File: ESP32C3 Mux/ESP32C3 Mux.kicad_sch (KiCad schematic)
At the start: 8 parts, among them J1 6130XX243121_613020243121, J2 Conn_01x02_Socket, U1 ESP32C3, U8 STLQ015M33R

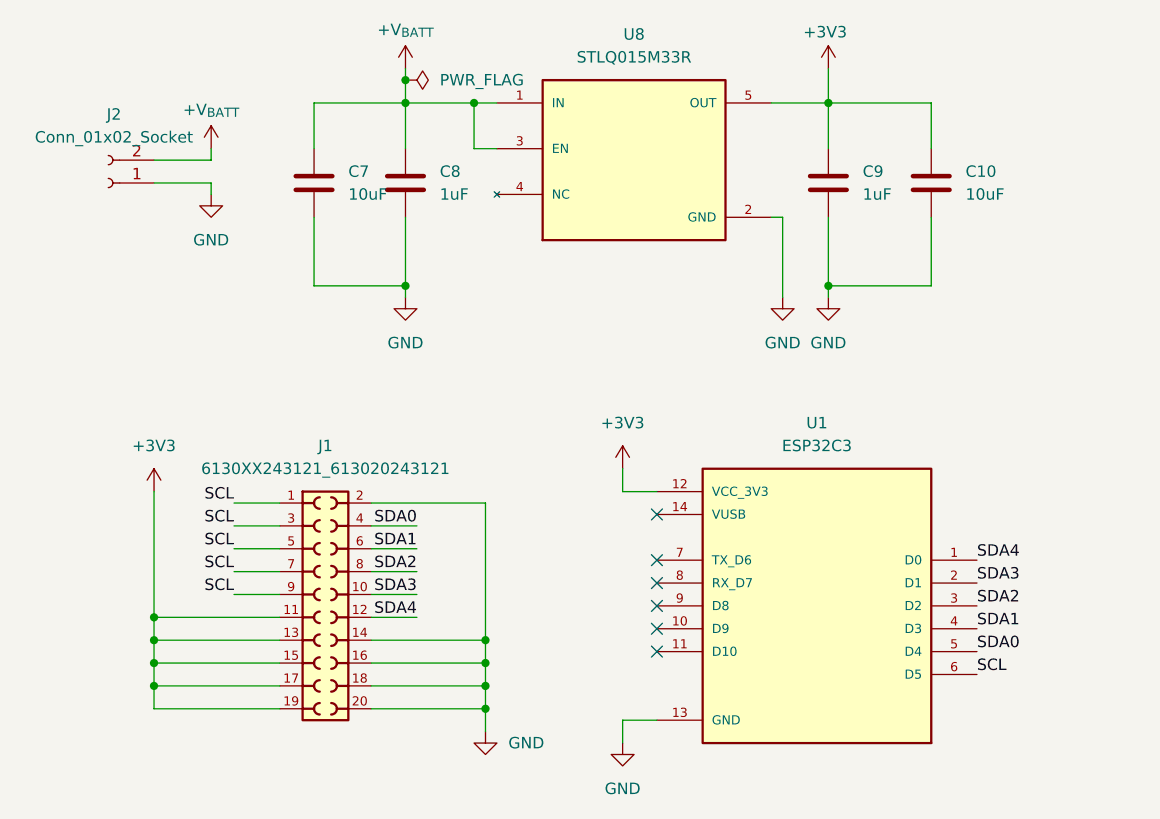
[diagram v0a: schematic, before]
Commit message: Fixed battery issues, removed LDOs
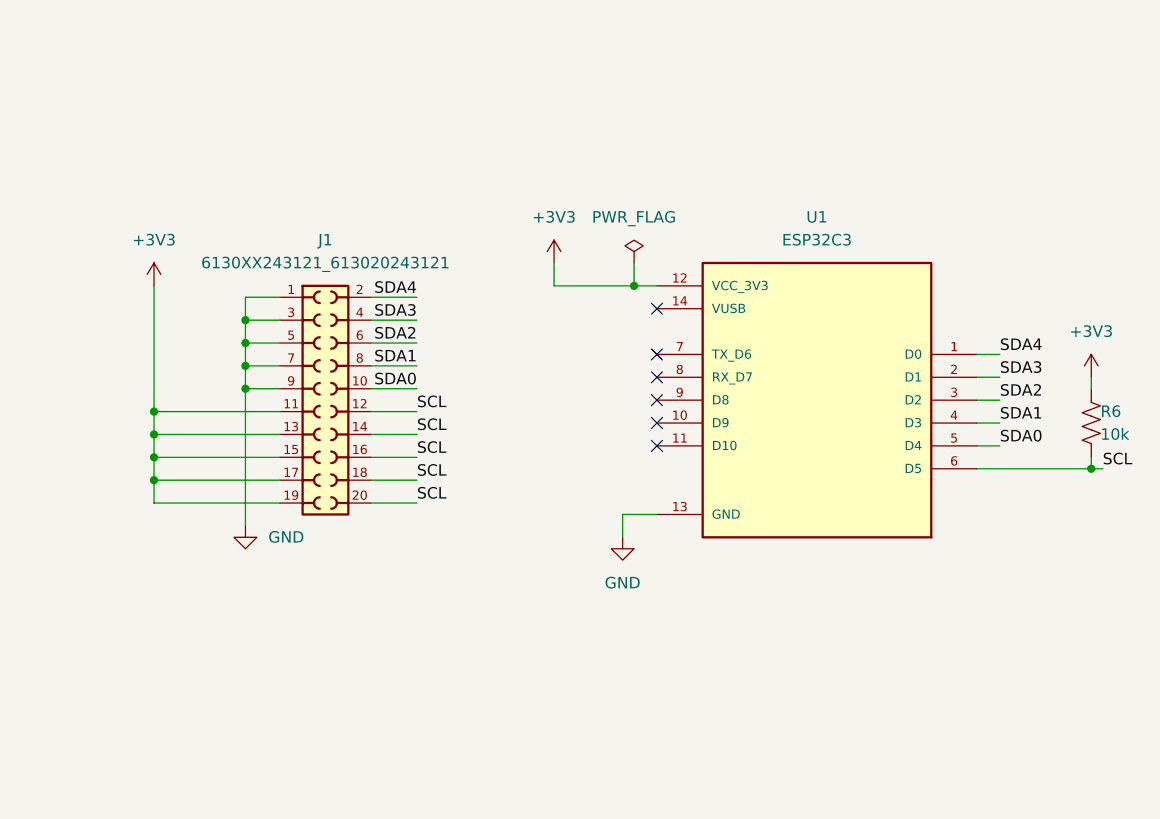
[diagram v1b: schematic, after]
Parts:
- removed C10, C7: 10uF, Capacitor_SMD:C_0805_2012Metric_Pad1.18x1.45mm_HandSolder, symbol Device:C
- removed C8, C9: 1uF, Capacitor_SMD:C_0805_2012Metric_Pad1.18x1.45mm_HandSolder, symbol Device:C
- removed J2: Conn_01x02_Socket, Connector_JST:JST_PH_B2B-PH-K_1x02_P2.00mm_Vertical, symbol Connector:Conn_01x02_Socket
- removed U8: STLQ015M33R, ESP32C3 Mux:SOT95P280X145-5N, symbol STLQ015M33R:STLQ015M33R
- added R6: 10k, Resistor_SMD:R_0603_1608Metric_Pad0.98x0.95mm_HandSolder, symbol Device:R_US
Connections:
- net +3V3: now also R6.1
- net GND: now also J1.1, J1.3, J1.5, J1.7, J1.9; no longer J1.14, J1.16, J1.18, J1.2, J1.20
- net SCL: now also J1.12, J1.14, J1.16, J1.18, J1.20, R6.2; no longer J1.1, J1.3, J1.5, J1.7, J1.9
- net SDA0: now also J1.10; no longer J1.4
- net SDA1: now also J1.8; no longer J1.6
- net SDA2: now also J1.6; no longer J1.8
- net SDA3: now also J1.4; no longer J1.10
- net SDA4: now also J1.2; no longer J1.12
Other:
- moved on the sheet: J1, U1
